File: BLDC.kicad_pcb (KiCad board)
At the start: 4 copper layers, 60 x 60 mm, 132 parts, among them J1 43650-0510, J2 436500313, J3 DNP, J4 43650-0510, U1 LMZ21700SIL, U12 MCP9808, U13 AS5047U, U17 INA250, U18 INA250, U19 INA250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

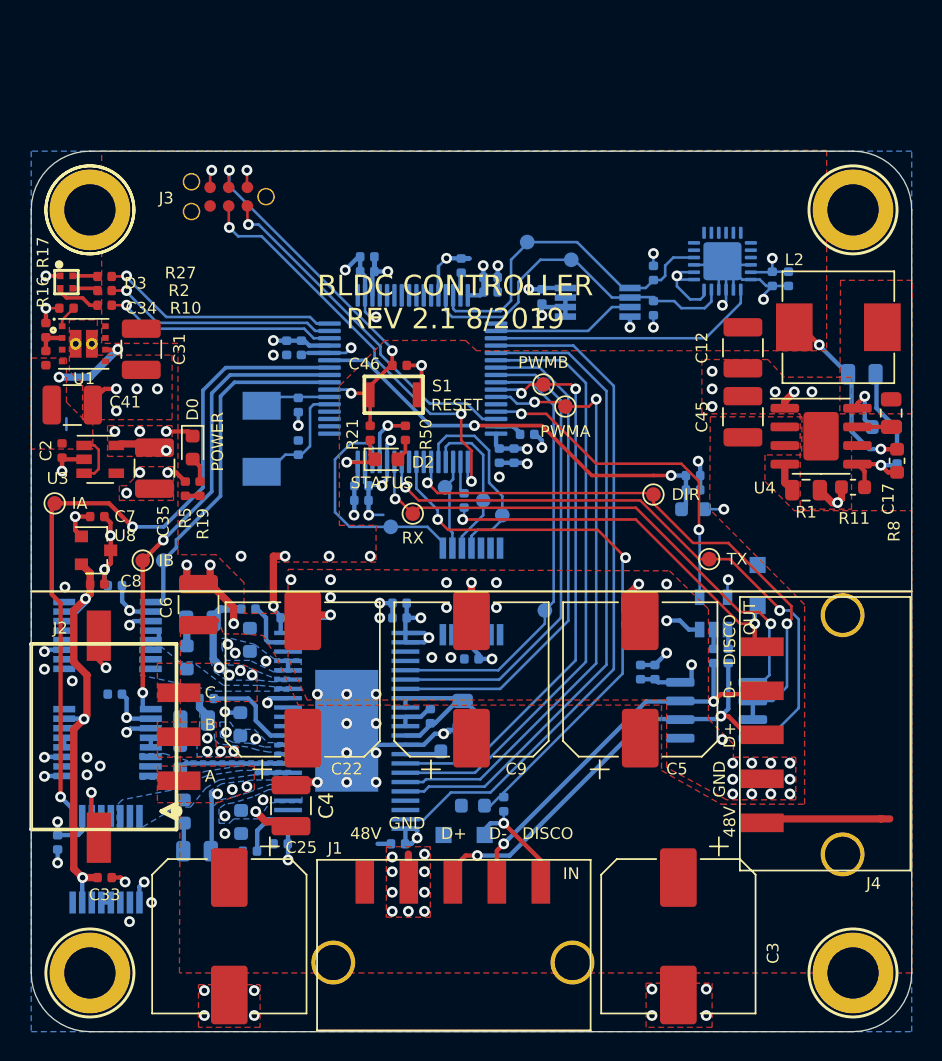
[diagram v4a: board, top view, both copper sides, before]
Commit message: WIP adding bonus header to north edge
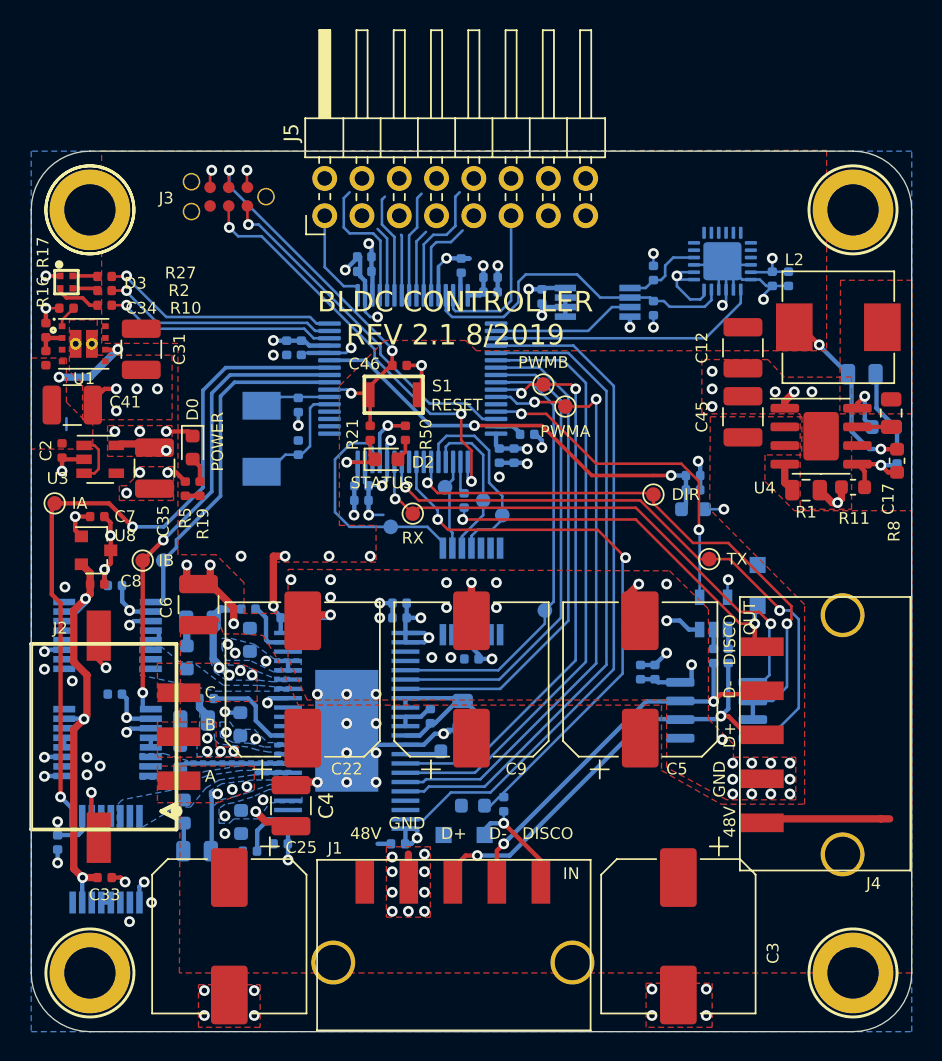
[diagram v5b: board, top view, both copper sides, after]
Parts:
- removed TP1, TP2: TestPoint, TestPoint:TestPoint_Pad_D1.0mm
- added J5: BONUS, Connector_PinHeader_2.54mm:PinHeader_2x08_P2.54mm_Horizontal, F.Cu at (138.5, 79.4)
- moved C24 0.20 mm to (141.2, 83.2)
- moved C27 0.20 mm to (141.2, 82.2)
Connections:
- U9 pad 17: Net-(U9-Pad17) -> /BONUS0
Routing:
- net Net-(U9-Pad20): track 0.00 -> 9.18 mm
- net Net-(U9-Pad26): track 0.00 -> 8.57 mm
- net Net-(U9-Pad24): track 0.00 -> 7.28 mm
- net Net-(U9-Pad22): track 0.00 -> 7.16 mm
- net /BONUS0: track 0.00 -> 6.90 mm
- net /I2C_SDA: track 23.2 -> 16.7 mm
- net Net-(U9-Pad27): track 0.00 -> 5.90 mm
- net Net-(U9-Pad21): track 0.00 -> 4.86 mm
- net Net-(U9-Pad25): track 0.00 -> 4.59 mm
- net Net-(U9-Pad23): track 0.00 -> 4.15 mm
- net /I2C_SCL: track 24.4 -> 23.2 mm
- net +3V3: track 65.6 -> 64.7 mm

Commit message: finish up bonus connector
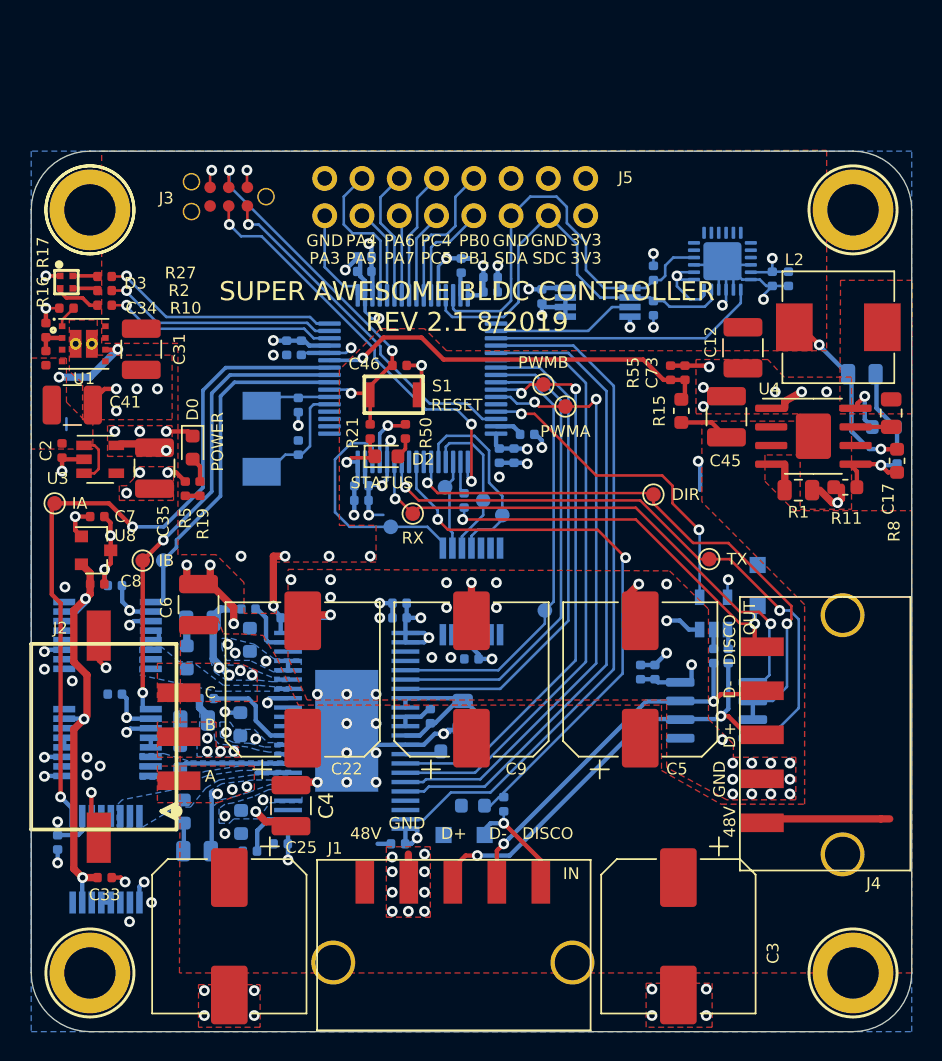
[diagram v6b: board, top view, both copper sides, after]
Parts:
- C73, R15, R55: moved to F.Cu
- moved R55 8.13 mm to (162.1, 90.1), turned to 90 degrees
- moved C73 7.03 mm to (163.0, 90.1), turned to 270 degrees
- moved R15 6.75 mm to (162.8, 92.7), turned to 90 degrees
- moved C45 1.13 mm to (165.9, 93.1)
- moved R1 0.53 mm to (170.8, 98.1)
- moved R11 0.53 mm to (174.0, 97.9)
- moved U4 0.53 mm to (171.8, 94.4)
- moved D2 0.20 mm to (142.7, 95.8)
- moved R21 0.10 mm to (141.6, 94.1)
- moved R50 0.10 mm to (144.0, 94.1)
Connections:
- J5 pad 10: Net-(J5-Pad10) -> /BONUS7
- J5 pad 12: Net-(J5-Pad12) -> GND
- J5 pad 3: Net-(J5-Pad3) -> /BONUS2
- J5 pad 4: Net-(J5-Pad4) -> /BONUS1
- J5 pad 5: Net-(J5-Pad5) -> /BONUS4
- J5 pad 6: Net-(J5-Pad6) -> /BONUS3
- J5 pad 7: Net-(J5-Pad7) -> /BONUS6
- J5 pad 8: Net-(J5-Pad8) -> /BONUS5
- J5 pad 9: Net-(J5-Pad9) -> /BONUS8
- U9 pad 20: Net-(U9-Pad20) -> /BONUS1
- U9 pad 21: Net-(U9-Pad21) -> /BONUS2
- U9 pad 22: Net-(U9-Pad22) -> /BONUS3
- U9 pad 23: Net-(U9-Pad23) -> /BONUS4
- U9 pad 24: Net-(U9-Pad24) -> /BONUS5
- U9 pad 25: Net-(U9-Pad25) -> /BONUS6
- U9 pad 26: Net-(U9-Pad26) -> /BONUS7
- U9 pad 27: Net-(U9-Pad27) -> /BONUS8
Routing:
- net /I2C_SDA: track 16.7 -> 29.7 mm
- net /BONUS1: track 0.00 -> 10.4 mm
- net /BONUS7: track 0.00 -> 9.99 mm
- net Net-(U9-Pad20): track 9.18 -> 0.00 mm
- net /BONUS3: track 0.00 -> 8.89 mm
- net /BONUS5: track 0.00 -> 8.74 mm
- net Net-(U9-Pad26): track 8.57 -> 0.00 mm
- net Net-(U9-Pad24): track 7.28 -> 0.00 mm
- net Net-(U9-Pad22): track 7.16 -> 0.00 mm
- net /BONUS8: track 0.00 -> 7.16 mm
- net /BONUS2: track 0.00 -> 6.30 mm
- net /BONUS6: track 0.00 -> 5.99 mm
- net /I2C_SCL: track 23.2 -> 29.1 mm
- net Net-(U9-Pad27): track 5.90 -> 0.00 mm
- net /BONUS4: track 0.00 -> 5.50 mm
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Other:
- board text added: "3V3"
- board text added: "PA3"
- board text added: "PA4"
- board text added: "PA5"
- board text added: "PA6"
- board text added: "PA7"
- board text added: "PB0"
- board text added: "PB1"
- board text added: "PC4"
- board text added: "PC5"
- board text added: "SDC"
- board text added: "SUPER AWESOME BLDC CONTROLLER REV 2.1 8/2019"
- board text removed: "BLDC CONTROLLER REV 2.1 8/2019"

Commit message: a bit more pcb cleanup, add slow-start cap MPN and gerbv project
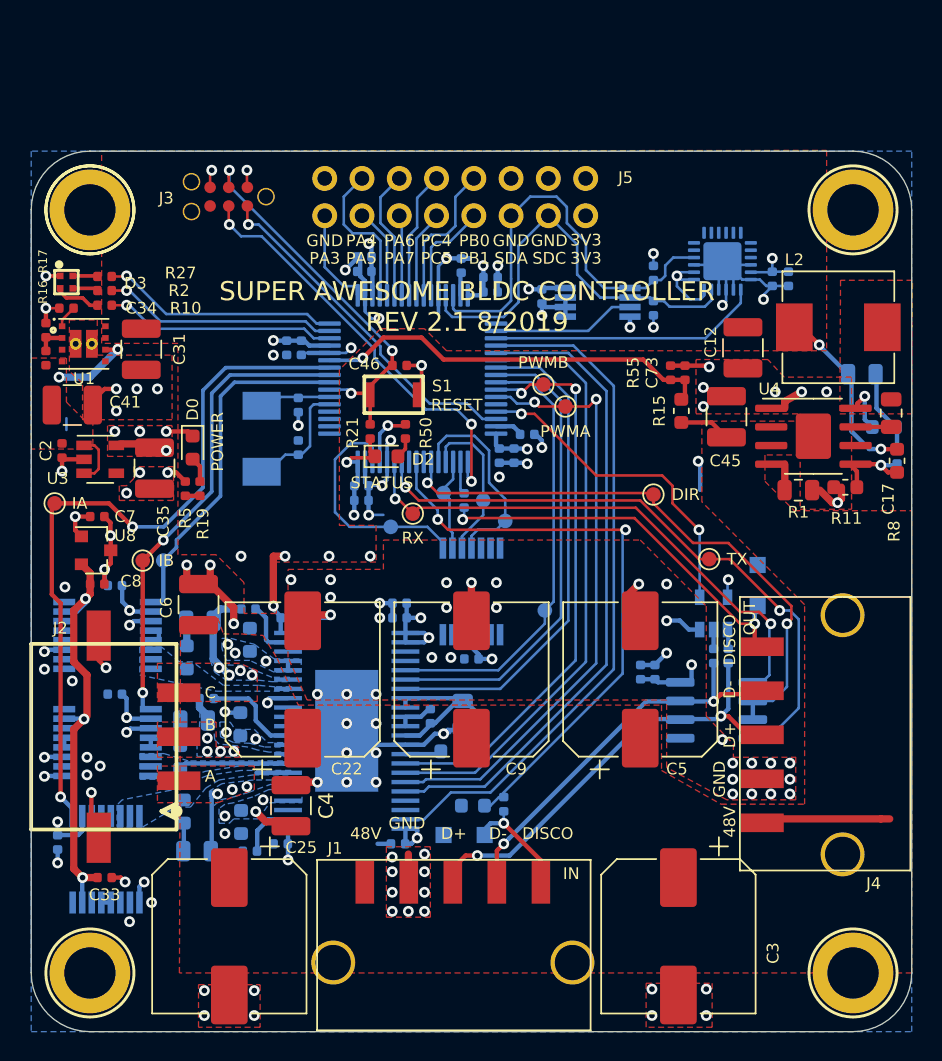
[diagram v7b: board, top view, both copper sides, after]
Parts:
- C34: value 3n3 -> 4n7
- moved TP3 0.45 mm to (150.8, 100.2)
- moved TP6 0.41 mm to (146.6, 98.3)
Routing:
- net GND: track 137.6 -> 138.8 mm
- net /DISCO_BUS_IN: track 39.6 -> 40.7 mm
